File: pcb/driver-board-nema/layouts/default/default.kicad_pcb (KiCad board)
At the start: 2 copper layers, 26 parts

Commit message: feat(pcb): place, route and pour the v2 NEMA driver board
62x76mm, 2 layers, DRC clean: 0 errors, 0 unconnected, 0 footprint errors.

GND is a two-layer pour rather than a routed net — it is the right answer
for a switching regulator, and it removes ~20 hand-routed segments. The
fill has to happen in KiCad, and `kicad-cli --save-board` rewrites the
file in a dialect faebryk cannot parse, so the filled board is a derived
artifact at build/filled.kicad_pcb and layouts/ stays atopile's.

Numeric checks caught what renders did not:
  * ss_right pin 8 is at x=39.89, not 40.89 — en_n was landing 1mm short
  * r_en_lo.1 is the -x pad; the route was starting on the GND pad
  * l_buck's pins were connected the wrong way round in main.ato
  * the motor connector is rotated 180, so its pads run B2 B1 A2 A1 left
    to right — the silk legend had it backwards and now labels each pad

step/dir/en_n leave the XIAO top-to-bottom but must arrive left-to-right
in the other order, which has no single-layer solution; each takes its
stub on F.Cu and its lane on B.Cu so the two cross on opposite layers.

tools/trim_lib_silk.py clips silk out of pads in the vendored libraries
(not on the board) so the board stays in parity with them. It refuses to
strip a footprint bare — doing so kills `ato build` in Geometry.bbox.

Claude-Session: https://claude.ai/code/session_01UQXFTEy3DeBEx85CfiBq9q
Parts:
- moved R8 232.9 mm to (19.0, 30.0)
- moved R7 185.9 mm to (55.0, 18.0)
- moved D1 176.3 mm to (55.0, 21.0)
- moved R2 172.0 mm to (39.5, 23.0)
- moved C1 165.6 mm to (58.0, 34.5)
- moved R1 161.7 mm to (39.5, 20.0)
- moved R4 151.0 mm to (43.0, 34.5)
- moved R3 140.7 mm to (43.0, 32.0)
- moved C4 121.5 mm to (53.5, 34.5)
- moved C3 116.7 mm to (48.5, 34.5)
- moved L1 100.9 mm to (53.5, 29.5)
- moved C5 97.9 mm to (46.0, 27.2)
- moved C7 93.1 mm to (40.5, 62.0)
- moved C2 83.0 mm to (50.5, 24.0), turned to 270 degrees
- moved U1 77.8 mm to (46.0, 24.0)
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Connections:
- C5 pad 2: sw_node -> 2-1
- D1 pad 2: 2-1 -> 2-2
- L1 pad 1: sw_node -> 1
- L1 pad 2: 1 -> 2-1
- R7 pad 2: 2-1 -> 2-2
- U1 pad 2: sw_node -> 2-1
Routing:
- net 1: track 0.00 -> 185.5 mm, vias 0 -> 1
- net 1-1: track 0.00 -> 93.1 mm, vias 0 -> 5
- net p3v3: track 0.00 -> 72.4 mm
- net hall_do: track 0.00 -> 71.7 mm
- net en_n: track 0.00 -> 67.2 mm, vias 0 -> 1
- net step: track 0.00 -> 51.5 mm, vias 0 -> 2
- net dir: track 0.00 -> 49.2 mm, vias 0 -> 2
- net v12_raw: track 0.00 -> 32.9 mm
- net m2b: track 0.00 -> 28.2 mm
- net 1-2: track 0.00 -> 27.7 mm, vias 0 -> 2
- net vfb: track 0.00 -> 20.1 mm, vias 0 -> 2
- net pdn: track 0.00 -> 19.4 mm
- net ven: track 0.00 -> 13.2 mm
- net m1a: track 0.00 -> 12.8 mm
- net 1-3: track 0.00 -> 12.6 mm, vias 0 -> 1
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- added copper zone on B.Cu, net 2
- added copper zone on F.Cu, net 2
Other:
- board outline added: 62 x 76 mm
- board text added: "+ CENTRE"
- board text added: "12V IN"
- board text added: "5V"
- board text added: "5V GND DO"
- board text added: "A1"
- board text added: "A2"
- board text added: "B1"
- board text added: "B2"
- board text added: "Designed by 0x63616c"
- board text added: "HALL"
- board text added: "MOTOR"
- board text added: "MS1 MS2 SPRD = GND"
- board text added: "NEMA 14 / TMC2209"
- board text added: "PDN=D6 (1k) HALL DO=D8"
- board text added: "PIN 1 / PIN 9 THIS END >"
- board text added: "SPLIT-FLAP DRIVER v2"
- board text added: "STEP=D0 DIR=D1 EN=D2"
- board text added: "TMC2209 StepStick"
- board text added: "USB ^"
- board text added: "VM BULK 470u"
- board text added: "XIAO ESP32-C6"

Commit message: fix(pcb-v2): swap male pin headers for female sockets
The XIAO and StepStick are modules with male pins soldered in, so the
board side has to be a receptacle. Kinghelm naming: PH = Pin Header
(male), FH = Female Header. Both socket parts were PH180, which would
have given four male headers that cannot mate with anything.

  1x7 (J6/J7, XIAO):      C2932700 PH180 -> C2932672 KH-2.54FH-1X7P-H8.5
  1x8 (J4/J5, StepStick): C2905487 PH180 -> C2905417 KH-2.54FH-1X8P-H8.5

Both verified in stock via the JLCPCB search API (2374 / 3941). Pad
geometry is identical between the two families -- pin 1 at -7.62/-8.89,
2.54mm pitch, 1.1mm drill, 1.7mm pads -- so this is a pure part swap
with no placement or routing impact. DRC unchanged at 1 (known-spurious)
warning, 0 unconnected.

Also correct trim_lib_silk.py's docstring: it claims to be idempotent and
is not. Each pass re-clips its own leftovers, so the outline erodes and
the file hash differs every run; an accidental second pass also desyncs
the layout from the library as an unclearable lib_footprint_mismatch.

Claude-Session: https://claude.ai/code/session_01UQXFTEy3DeBEx85CfiBq9q
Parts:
- J4, J5: footprint KH_2_54_1X8_FEMALE:HDR-TH_8P-P2.54-V-M -> KH_2_54_1X8_FEMALE:HDR-TH_8P-P2.54-V-F
- J6, J7: footprint KH_2_54_1X7_FEMALE:HDR-TH_7P-P2.54-V-M -> KH_2_54_1X7_FEMALE:HDR-TH_7P-P2.54-V-F

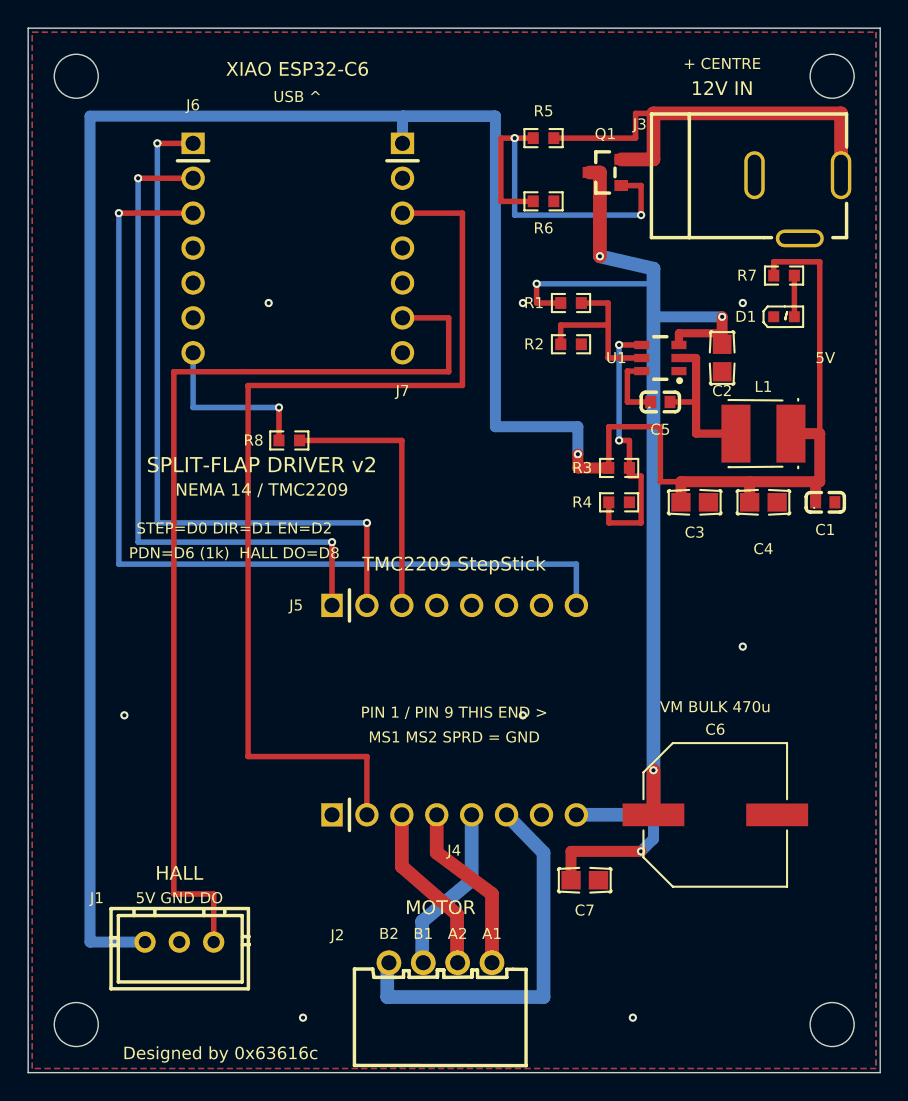
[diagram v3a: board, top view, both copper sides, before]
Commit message: fix(pcb-v2): reverse-polarity FET, socket pitch, and the review backlog
Two independent reviews found a board that builds and passes DRC but
would not work. The blockers:

B1 StepStick socket rows were 15.24mm apart. The 0.6x0.8in figure for a
   StepStick is its BOARD OUTLINE; the pin rows are inset 1.27mm per
   side, so the pitch is 12.70mm. The module physically could not seat.
   ss_right moves 42.00 -> 44.54 (ss_left stays, so the motor block and
   VM bulk keep their routing) and check_socket_pitch() now asserts both
   pitches numerically at place time -- this is the class of error that
   nothing else in the flow catches.

B2 Q1's source and drain were swapped. A P-FET body diode conducts
   drain->source, so with the source on the jack side it stayed forward
   biased under reverse input: reverse current flowed anyway and put
   about -11.3V across the 470uF electrolytic. Drain now faces the jack,
   source the rail, and the gate divider follows the source onto v12.

B3 The pin-1 arrow pointed at pin 8/16. Both rows are identical 1x8
   headers, so that arrow was the only thing preventing a destructive
   180-degree insertion. Direction fixed and each row now also carries
   what it is ("J4 VM + COILS", "J5 LOGIC").

Should-fix, all applied: 3A barrel jack (S1); D7/U0RXD tied to PDN so
the UART can be read and not just written (S2); 1k in the hall DO line
(S3); 100pF Cff across the feedback high side with 56k -> 54.9k, TI
SLVAF45's own values for this exact 12V->5V case (S4); a third output
cap, since 2x22uF X5R derates to ~20-24uF against TI's 20-68uF window
(S5); a series Schottky to the XIAO's 5V pad, which is its USB VBUS net,
with the hall supply deliberately tapped upstream (S6); silk normalised
to >=0.15mm and refdes to 1.0mm (S7); an explicit "+" beside C6, whose
footprint chamfer marks the positive end and so reads backwards to
anyone going by the can's stripe (S8); 0.05mm mask expansion (S9); M3
holes as real NPTH pads, so they land in the drill 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
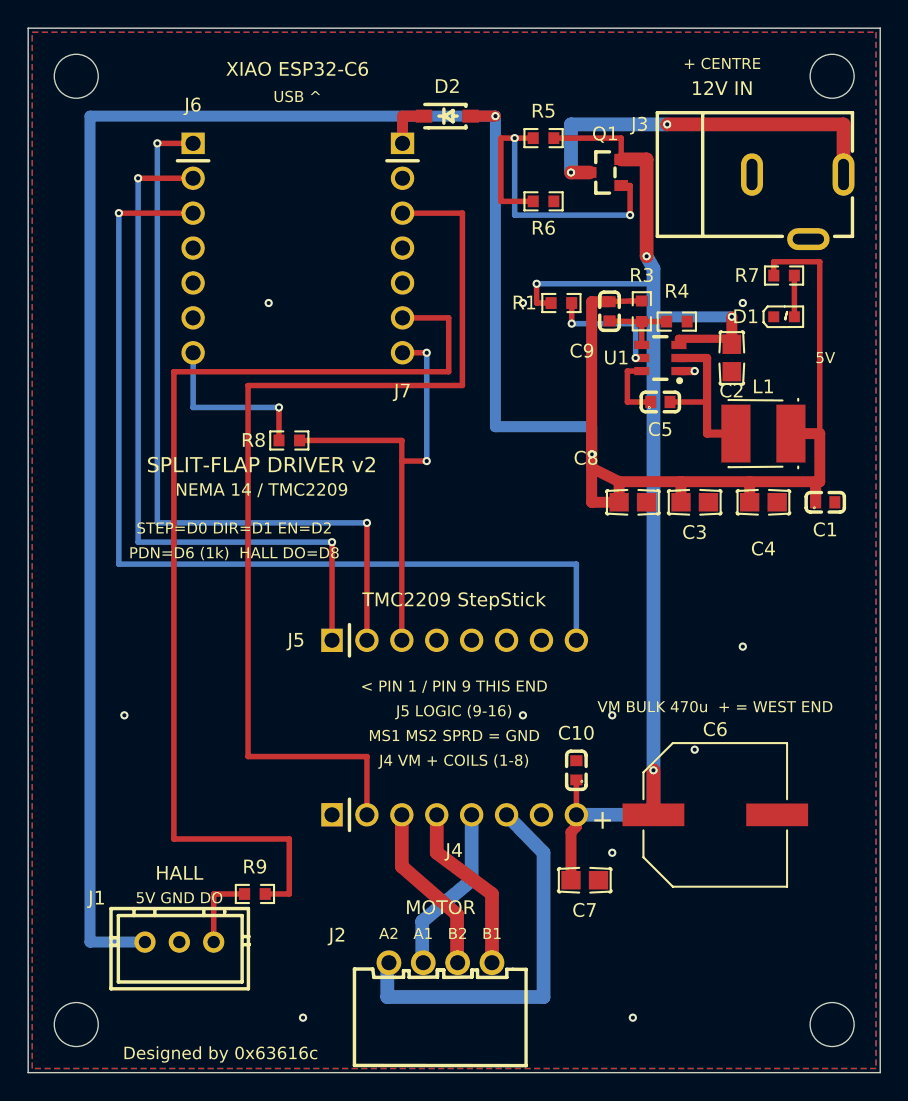
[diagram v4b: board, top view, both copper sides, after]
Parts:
- removed R2: , R0603_56K:R0603
- added ?: , SPLITFLAP_MOUNT:M3_NPTH, F.Cu at (3.50, 3.50)
- added ?: , SPLITFLAP_MOUNT:M3_NPTH, F.Cu at (58.5, 3.50)
- added ?: , SPLITFLAP_MOUNT:M3_NPTH, F.Cu at (3.50, 72.5)
- added ?: , SPLITFLAP_MOUNT:M3_NPTH, F.Cu at (58.5, 72.5)
- added C10: , CC0603_100NF:C0603, F.Cu at (39.9, 54.0)
- added C8: , CAP0805_22UF_25V:C0805, F.Cu at (44.0, 34.5)
- added C9: , CC0603_100PF:C0603, F.Cu at (42.3, 20.6)
- added D2: , D_B5819W:SOD-123_L2.7-W1.6-LS3.7-RD-1, F.Cu at (30.5, 6.40)
- added R9: , R0603_1K:R0603, F.Cu at (16.5, 63.0)
- J3: footprint DC_005:DC-IN-TH_DC-005-5.5-2.0 -> DC_005C:DC-IN-TH_DC-005C-20A
- R3: footprint R0603_56K:R0603 -> R0603_54K9:R0603
- moved R4 13.8 mm to (47.2, 21.4)
- moved R3 11.5 mm to (44.6, 20.6), turned to 270 degrees
- moved J5 2.54 mm to (31.0, 44.5)
- moved C2 0.70 mm to (51.2, 24.0)
- moved R1 0.70 mm to (38.8, 20.0)
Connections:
- J1 pad 3: hall_do -> hall_raw
- J7 pad 1: 1 -> p5v_xiao
- J7 pad 7: 7 -> pdn
- Q1 pad 2: v12_raw -> 1-1
- Q1 pad 3: 1-1 -> v12_raw
- R5 pad 2: v12_raw -> 1-1
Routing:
- net vfb: track 20.1 -> 5.85 mm, vias 2 -> 0
- net pdn: track 19.4 -> 33.4 mm, vias 0 -> 2
- net 1: track 185.5 -> 193.5 mm, vias 1 -> 2
- net hall_raw: track 0.00 -> 5.75 mm
- net v12_raw: track 32.9 -> 28.3 mm, vias 0 -> 2
- net ven: track 13.2 -> 9.10 mm, vias 0 -> 2
- net hall_do: track 71.7 -> 75.4 mm
- net p5v_xiao: track 0.00 -> 3.54 mm
- net 1-1: track 93.1 -> 95.8 mm, vias 5 -> 4
- net en_n: track 67.2 -> 69.8 mm
- net step: track 51.5 -> 54.0 mm
- net dir: track 49.2 -> 51.7 mm
- net 1-2: track 27.7 -> 26.1 mm
- net 2: track 0.00 -> 1.15 mm, vias 8 -> 12
- net 2-1: track 11.5 -> 12.3 mm
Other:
- outline, holes or cut-outs redrawn
- rule pad_to_mask_clearance: 0 -> 0.05
- board text added: "+"
- board text added: "< PIN 1 / PIN 9 THIS END"
- board text added: "J4 VM + COILS (1-8)"
- board text added: "J5 LOGIC (9-16)"
- board text added: "VM BULK 470u + = WEST END"
- board text removed: "PIN 1 / PIN 9 THIS END >"
- board text removed: "VM BULK 470u"
